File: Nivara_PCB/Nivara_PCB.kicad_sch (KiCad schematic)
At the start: 12 parts, among them J1 NPN_IN, J10 PNP_OUT, J11 Analog_Out, J2 PNP_IN, J3 D_IN, J4 NPN_OUT, J5 RELAY, J6 RUN/STOP, J7 FUENTE, J8 RS485, J9 Analaog_In

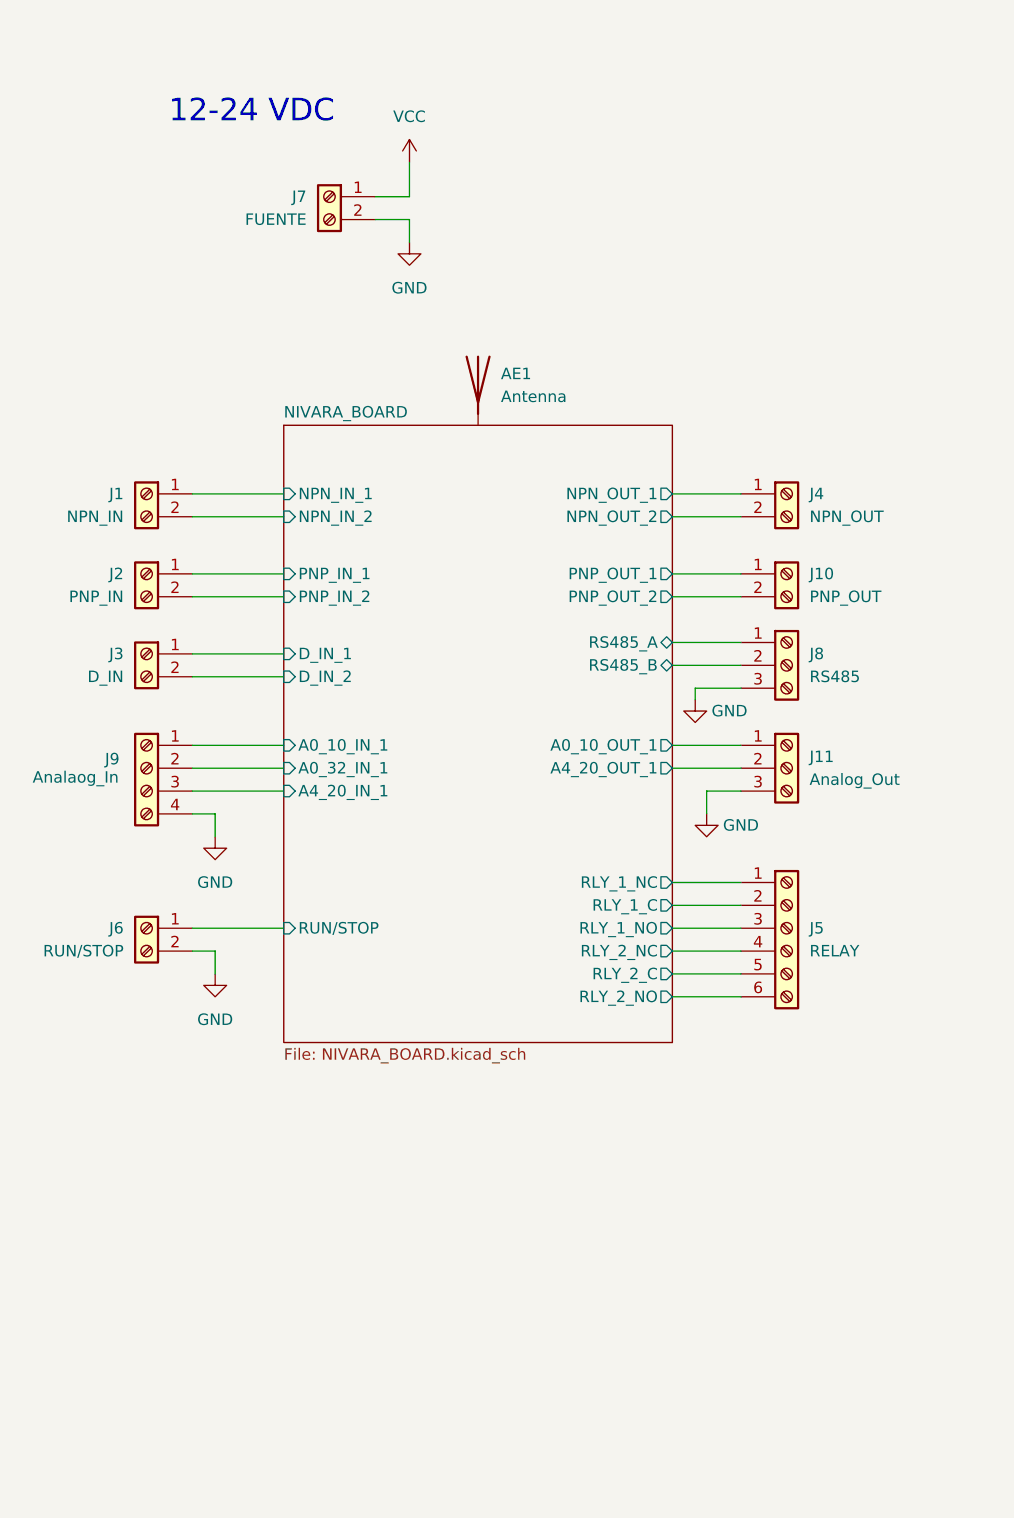
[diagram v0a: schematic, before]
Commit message: Añadido de funciones NPN/PNP
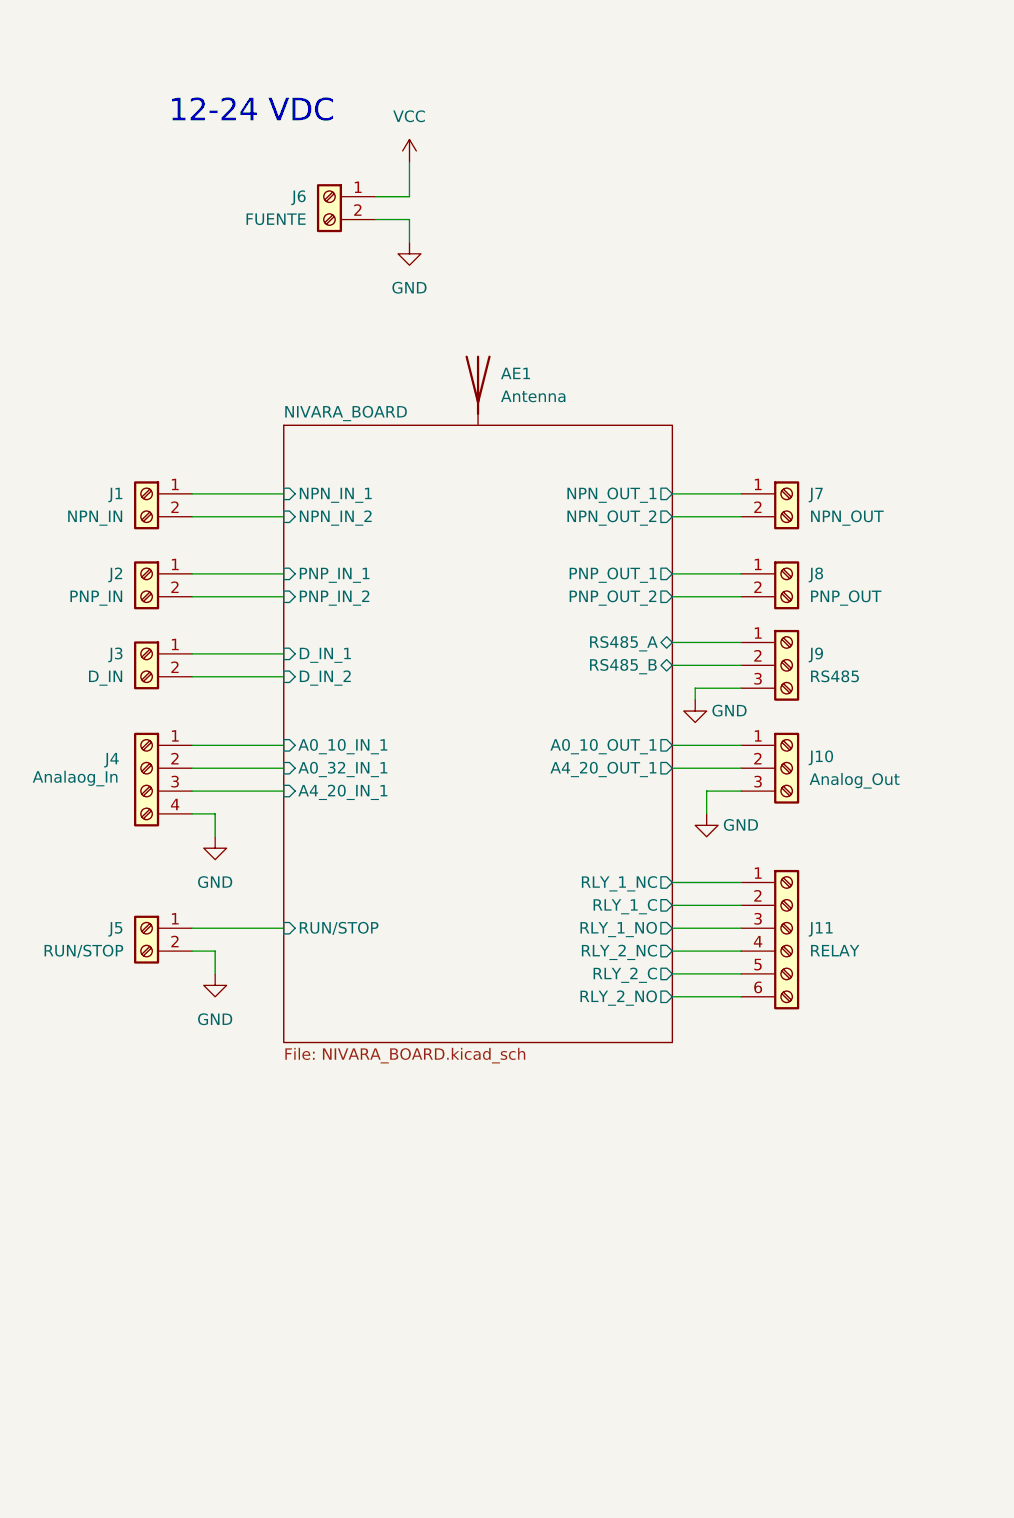
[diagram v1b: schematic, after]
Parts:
- renumbered J11 to J10, J5 to J11, J9 to J4, J6 to J5, J7 to J6, J4 to J7, J10 to J8, J8 to J9
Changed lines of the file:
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@@
+		(dnp no)
+		(fields_autoplaced yes)
+		(property "Reference" "#PWR03"
+			(at 54.61 35.56 0)
+			(effects
+				(font
+					(size 1.27 1.27)
+				)
+				(hide yes)
+			)
+		)
+		(property "Value" "VCC"
+			(at 54.61 26.67 0)
+			(effects
+				(font
+					(size 1.27 1.27)
+				)
+			)
+		)
+		(property "Footprint" ""
+			(at 54.61 31.75 0)
+			(effects
+				(font
+					(size 1.27 1.27)
+				)
+				(hide yes)
+			)
+		)
+		(property "Datasheet" ""
+			(at 54.61 31.75 0)
+			(effects
+				(font
+					(size 1.27 1.27)
+				)
+				(hide yes)
+			)
+		)
+		(property "Description" "Power symbol creates a global label with name \"VCC\""
+			(at 54.61 31.75 0)
+			(effects
+				(font
+					(size 1.27 1.27)
+				)
+				(hide yes)
+			)
+		)
+		(pin "1"
+		)
+		(instances
+			(project ""
+				(path "/13184db0-a71d-4054-b13a-bbf46d2b100d"
+					(reference "#PWR03")
+					(unit 1)
+				)
+			)
+		)
+	)
+	(symbol
+		(lib_id "power:GND")
+		(at 33.02 106.68 0)
+		(unit 1)
+		(exclude_from_sim no)
+		(in_bom yes)
+		(on_board yes)
 		(dnp no)
 		(fields_autoplaced yes)
 		(property "Reference" "#PWR01"
-			(at 54.61 35.56 0)
-			(effects
-				(font
-					(size 1.27 1.27)
-				)
-				(hide yes)
-			)
-		)
-		(property "Value" "VCC"
-			(at 54.61 26.67 0)
-			(effects
-				(font
-					(size 1.27 1.27)
-				)
-			)
-		)
-		(property "Footprint" ""
-			(at 54.61 31.75 0)
-			(effects
-				(font
-					(size 1.27 1.27)
-				)
-				(hide yes)
-			)
-		)
-		(property "Datasheet" ""
-			(at 54.61 31.75 0)
-			(effects
-				(font
-					(size 1.27 1.27)
-				)
-				(hide yes)
-			)
-		)
-		(property "Description" "Power symbol creates a global label with name \"VCC\""
-			(at 54.61 31.75 0)
-			(effects
-				(font
-					(size 1.27 1.27)
-				)
-				(hide yes)
-			)
-		)
-		(pin "1"
-		)
-		(instances
-			(project ""
-				(path "/13184db0-a71d-4054-b13a-bbf46d2b100d"
-					(reference "#PWR01")
-					(unit 1)
-				)
-			)
-		)
-	)
-	(symbol
-		(lib_id "power:GND")
-		(at 33.02 106.68 0)
-		(unit 1)
-		(exclude_from_sim no)
-		(in_bom yes)
-		(on_board yes)
-		(dnp no)
-		(fields_autoplaced yes)
-		(property "Reference" "#PWR06"
 			(at 33.02 113.03 0)
 			(effects
@@
 			(project "Nivara_PCB"
 				(path "/13184db0-a71d-4054-b13a-bbf46d2b100d"
-					(reference "#PWR06")
+					(reference "#PWR01")
 					(unit 1)
 				)
@@
 		(on_board yes)
 		(dnp no)
-		(property "Reference" "#PWR08"
+		(property "Reference" "#PWR06"
 			(at 87.63 110.49 0)
 			(effects
@@
 			(project "Nivara_PCB"
 				(path "/13184db0-a71d-4054-b13a-bbf46d2b100d"
-					(reference "#PWR08")
+					(reference "#PWR06")
 					(unit 1)
 				)
@@
 		(on_board yes)
 		(dnp no)
-		(property "Reference" "J4"
+		(property "Reference" "J7"
 			(at 99.06 68.5799 0)
 			(effects
@@
 			(project ""
 				(path "/13184db0-a71d-4054-b13a-bbf46d2b100d"
-					(reference "J4")
+					(reference "J7")
 					(unit 1)
 				)
@@
 		(on_board yes)
 		(dnp no)
-		(property "Reference" "J6"
+		(property "Reference" "J5"
 			(at 22.86 116.8399 0)
 			(effects
@@
 			(project "Nivara_PCB"
 				(path "/13184db0-a71d-4054-b13a-bbf46d2b100d"
-					(reference "J6")
+					(reference "J5")
 					(unit 1)
 				)
@@
 		(on_board yes)
 		(dnp no)
-		(property "Reference" "J7"
+		(property "Reference" "J6"
 			(at 43.18 35.5599 0)
 			(effects
@@
 			(project "Nivara_PCB"
 				(path "/13184db0-a71d-4054-b13a-bbf46d2b100d"
-					(reference "J7")
+					(reference "J6")
 					(unit 1)
 				)
@@
 		(dnp no)
 		(fields_autoplaced yes)
-		(property "Reference" "#PWR07"
+		(property "Reference" "#PWR02"
 			(at 33.02 128.27 0)
 			(effects
@@
 			(project "Nivara_PCB"
 				(path "/13184db0-a71d-4054-b13a-bbf46d2b100d"
-					(reference "#PWR07")
+					(reference "#PWR02")
 					(unit 1)
 				)
@@
 		(on_board yes)
 		(dnp no)
-		(property "Reference" "J5"
+		(property "Reference" "J11"
 			(at 99.06 116.8399 0)
 			(effects
@@
 			(project ""
 				(path "/13184db0-a71d-4054-b13a-bbf46d2b100d"
-					(reference "J5")
+					(reference "J11")
 					(unit 1)
 				)
@@
 		(dnp no)
 		(fields_autoplaced yes)
-		(property "Reference" "#PWR02"
+		(property "Reference" "#PWR04"
 			(at 54.61 46.99 0)
 			(effects
@@
 			(project ""
 				(path "/13184db0-a71d-4054-b13a-bbf46d2b100d"
-					(reference "#PWR02")
+					(reference "#PWR04")
 					(unit 1)
 				)
@@
 		(dnp no)
 		(fields_autoplaced yes)
-		(property "Reference" "J11"
+		(property "Reference" "J10"
 			(at 99.06 97.7899 0)
 			(effects
@@
 			(project "Nivara_PCB"
 				(path "/13184db0-a71d-4054-b13a-bbf46d2b100d"
-					(reference "J11")
+					(reference "J10")
 					(unit 1)
 				)
@@
 		(dnp no)
 		(fields_autoplaced yes)
-		(property "Reference" "J8"
+		(property "Reference" "J9"
 			(at 99.06 86.3599 0)
 			(effects
@@
 			(project ""
 				(path "/13184db0-a71d-4054-b13a-bbf46d2b100d"
-					(reference "J8")
+					(reference "J9")
 					(unit 1)
 				)
@@
 		(on_board yes)
 		(dnp no)
-		(property "Reference" "J9"
+		(property "Reference" "J4"
 			(at 21.59 98.044 0)
 			(effects
@@
 			(project ""
 				(path "/13184db0-a71d-4054-b13a-bbf46d2b100d"
-					(reference "J9")
+					(reference "J4")
 					(unit 1)
 				)
@@
 		(on_board yes)
 		(dnp no)
-		(property "Reference" "J10"
+		(property "Reference" "J8"
 			(at 99.06 77.4699 0)
 			(effects
@@
 			(project "Nivara_PCB"
 				(path "/13184db0-a71d-4054-b13a-bbf46d2b100d"
-					(reference "J10")
-					(unit 1)
-				)
+					(reference "J8")
+					(unit 1)
+				)

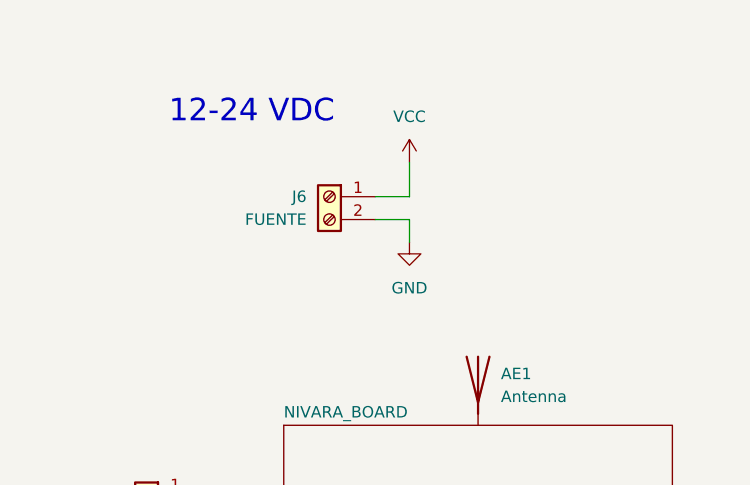
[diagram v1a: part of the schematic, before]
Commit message: Añadido de diodo TVS y resetteable fuse.
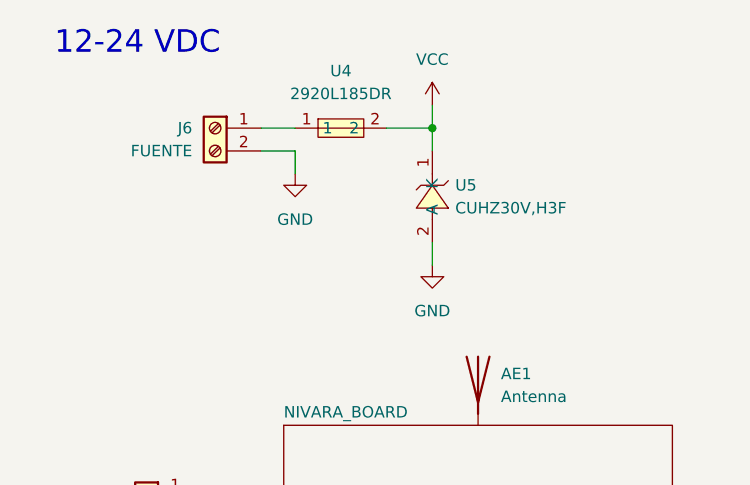
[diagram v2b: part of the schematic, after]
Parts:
- added U4: 2920L185DR, Fuse_Holder:F2920, symbol Fuse_Holder:2920L185DR
- added U5: CUHZ30V,H3F, Fuse_Holder:SOD-323HE_L2.0-W1.4-LS2.5-RD, symbol Fuse_Holder:CUHZ30V,H3F
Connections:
- net GND: now also U5.2 (A)
- net VCC: now also U4.2, U5.1 (K); no longer J6.1 (Pin_1)
- new net: J6.1 (Pin_1), U4.1
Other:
- moved on the sheet: J6

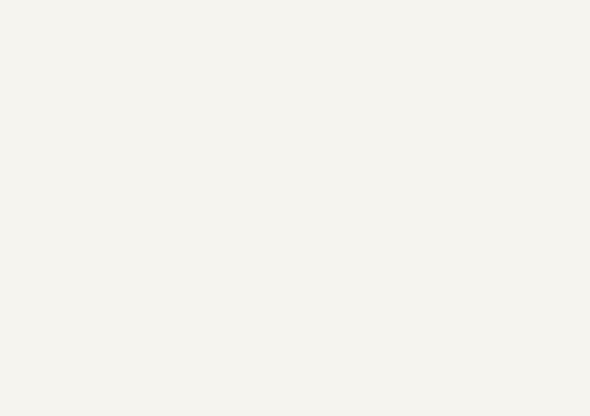
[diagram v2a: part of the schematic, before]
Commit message: Ajuste de RS-485 y protección de alimentación contra cortocircuito y sobre voltaje.
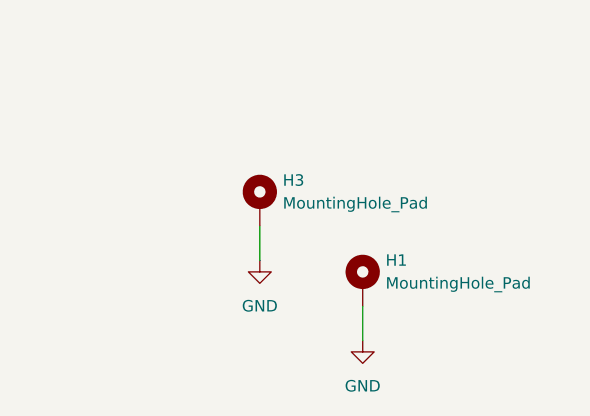
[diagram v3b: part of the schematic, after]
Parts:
- added H1, H3: MountingHole_Pad, MountingHole:MountingHole_3.2mm_M3_Pad_Via, symbol Mechanical:MountingHole_Pad
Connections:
- net GND: now also H1.1, H3.1
